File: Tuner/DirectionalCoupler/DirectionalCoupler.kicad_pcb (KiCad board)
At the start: 2 copper layers, 100 x 100 mm, 71 parts, among them J1 Conn_01x02, J10 Conn_01x01, J11 Conn_01x01, J12 Conn_01x01, J13 Conn_01x01, J14 Conn_01x01, J15 Conn_01x01, J16 Conn_01x01, J17 Barrel_Jack, J18 Conn_Coaxial, J19 Conn_01x02, J2 Conn_01x02, J20 Conn_Coaxial, J21 Conn_01x01, J22 Conn_01x01, J23 Conn_01x01, J24 Conn_01x01, J25 Conn_01x01, J26 Conn_01x01, J27 Conn_01x01, J28 Conn_01x01, J29 Conn_01x01, J3 Conn_Coaxial, J30 Conn_01x01, J31 Conn_01x01, J32 Conn_01x01, J33 Conn_01x03, J4 Conn_Coaxial, J5 Conn_01x01, J6 Conn_01x01, J7 Conn_01x01, J8 Conn_01x01, J9 Conn_01x01

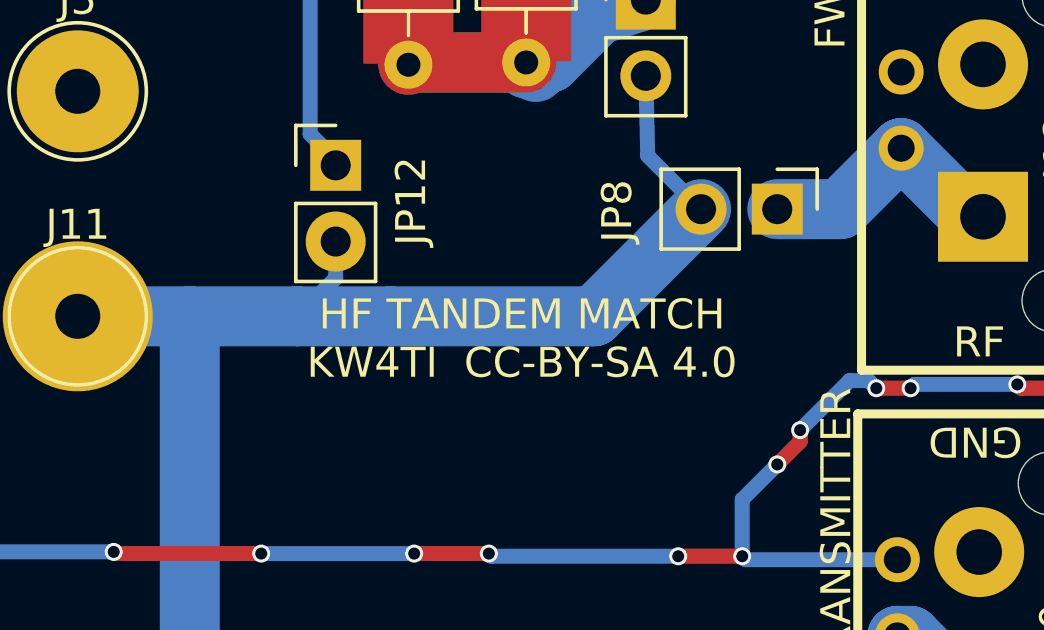
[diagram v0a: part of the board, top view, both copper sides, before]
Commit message: Change named to DirectionalCoupler, fixed order of two pins in QuadCoupler
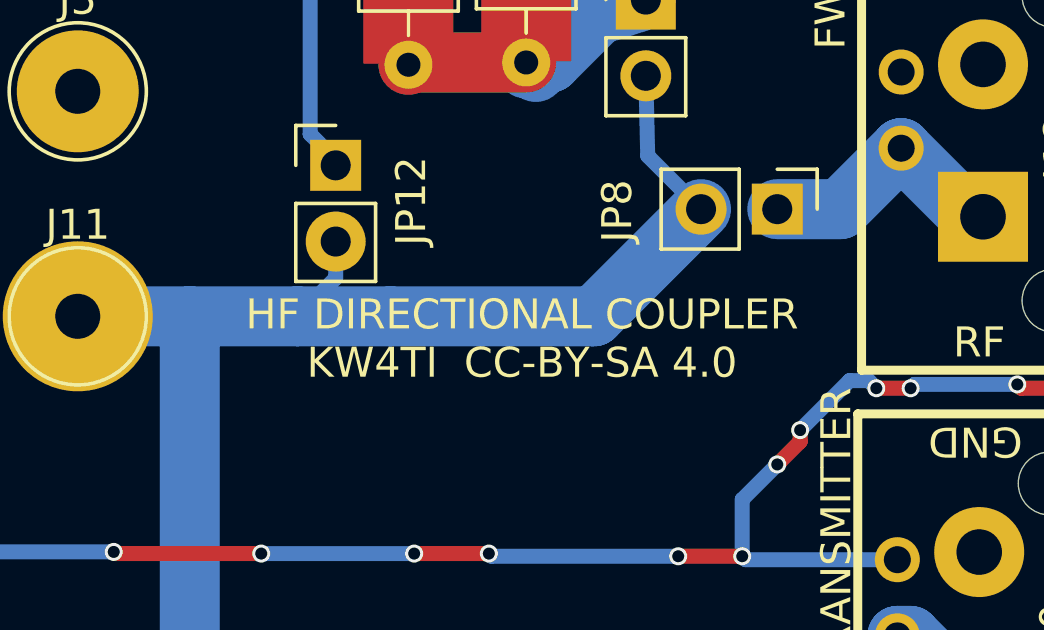
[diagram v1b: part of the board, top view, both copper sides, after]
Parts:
- F1: footprint TandemMatch:SL506Pfuseholder -> DirectionalCoupler:SL506Pfuseholder
- J18, J20, J3, J4: footprint TandemMatch:bnc_90_1-1337543-0_pad_combo -> DirectionalCoupler:bnc_90_1-1337543-0_pad_combo
- L1: footprint TandemMatch:BigRFChokeInductor -> DirectionalCoupler:BigRFChokeInductor
- R1, R2, R3, R4: footprint TandemMatch:R_Axial_DIN0309_L9.0mm_D3.2mm_P12.70mm_Horizontal -> DirectionalCoupler:R_Axial_DIN0309_L9.0mm_D3.2mm_P12.70mm_Horizontal
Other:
- board text added: "HF DIRECTIONAL COUPLER KW4TI CC-BY-SA 4.0"
- board text removed: "HF TANDEM MATCH KW4TI CC-BY-SA 4.0"
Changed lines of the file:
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@@
     (add_net "Net-(JP6-Pad1)")
   )
-  (module TandemMatch:bnc_90_1-1337543-0_pad_combo (layer F.Cu)
+  (module DirectionalCoupler:bnc_90_1-1337543-0_pad_combo (layer F.Cu)
     (at 40.386 56.769 270)
     (descr "BNC connector, Tyco 1-1337543-0")
@@
     )
   )
-  (module TandemMatch:R_Axial_DIN0309_L9.0mm_D3.2mm_P12.70mm_Horizontal (layer F.Cu)
+  (module DirectionalCoupler:R_Axial_DIN0309_L9.0mm_D3.2mm_P12.70mm_Horizontal (layer F.Cu)
     (at 111.0234 41.4147 270)
     (descr "Resistor, Axial_DIN0309 series, Axial, Horizontal, pin pitch=12.7mm, 0.5W = 1/2W, length*diameter=9*3.2mm^2, http://cdn-reichelt.de/documents/datenblatt/B400/1_4W%23YAG.pdf")
@@
     )
   )
-  (module TandemMatch:R_Axial_DIN0309_L9.0mm_D3.2mm_P12.70mm_Horizontal (layer F.Cu)
+  (module DirectionalCoupler:R_Axial_DIN0309_L9.0mm_D3.2mm_P12.70mm_Horizontal (layer F.Cu)
     (at 114.9477 41.3385 270)
     (descr "Resistor, Axial_DIN0309 series, Axial, Horizontal, pin pitch=12.7mm, 0.5W = 1/2W, length*diameter=9*3.2mm^2, http://cdn-reichelt.de/documents/datenblatt/B400/1_4W%23YAG.pdf")
@@
     )
   )
-  (module TandemMatch:R_Axial_DIN0309_L9.0mm_D3.2mm_P12.70mm_Horizontal (layer F.Cu)
+  (module DirectionalCoupler:R_Axial_DIN0309_L9.0mm_D3.2mm_P12.70mm_Horizontal (layer F.Cu)
     (at 66.4464 42.0243 270)
     (descr "Resistor, Axial_DIN0309 series, Axial, Horizontal, pin pitch=12.7mm, 0.5W = 1/2W, length*diameter=9*3.2mm^2, http://cdn-reichelt.de/documents/datenblatt/B400/1_4W%23YAG.pdf")
@@
     )
   )
-  (module TandemMatch:R_Axial_DIN0309_L9.0mm_D3.2mm_P12.70mm_Horizontal (layer F.Cu)
+  (module DirectionalCoupler:R_Axial_DIN0309_L9.0mm_D3.2mm_P12.70mm_Horizontal (layer F.Cu)
     (at 62.484 41.9862 270)
     (descr "Resistor, Axial_DIN0309 series, Axial, Horizontal, pin pitch=12.7mm, 0.5W = 1/2W, length*diameter=9*3.2mm^2, http://cdn-reichelt.de/documents/datenblatt/B400/1_4W%23YAG.pdf")
@@
     )
   )
-  (module TandemMatch:SL506Pfuseholder (layer F.Cu)
+  (module DirectionalCoupler:SL506Pfuseholder (layer F.Cu)
     (at 112.0775 109.093 270)
     (fp_text reference F1 (at 0 0 360) (layer F.SilkS)
@@
     )
   )
-  (module TandemMatch:BigRFChokeInductor (layer F.Cu)
+  (module DirectionalCoupler:BigRFChokeInductor (layer F.Cu)
     (at 130.302 107.95 90)
     (fp_text reference L1 (at -11 3 90) (layer F.SilkS)
@@
     (pad "" np_thru_hole circle (at 0 6 90) (size 4 4) (drill 4) (layers *.Cu *.Mask))
   )
-  (module TandemMatch:bnc_90_1-1337543-0_pad_combo (layer F.Cu)
+  (module DirectionalCoupler:bnc_90_1-1337543-0_pad_combo (layer F.Cu)
     (at 40.259 73.406 270)
     (descr "BNC connector, Tyco 1-1337543-0")
@@
     )
   )
-  (module TandemMatch:bnc_90_1-1337543-0_pad_combo (layer F.Cu)
+  (module DirectionalCoupler:bnc_90_1-1337543-0_pad_combo (layer F.Cu)
     (at 139.827 56.896 90)
     (descr "BNC connector, Tyco 1-1337543-0")
@@
     )
   )
-  (module TandemMatch:bnc_90_1-1337543-0_pad_combo (layer F.Cu)
+  (module DirectionalCoupler:bnc_90_1-1337543-0_pad_combo (layer F.Cu)
     (at 139.7 73.152 90)
     (descr "BNC connector, Tyco 1-1337543-0")
@@
     (effects (font (size 1 1) (thickness 0.15)))
   )
-  (gr_text "HF TANDEM MATCH\nKW4TI  CC-BY-SA 4.0" (at 114.808 63.246) (layer F.SilkS)
+  (gr_text "HF DIRECTIONAL COUPLER\nKW4TI  CC-BY-SA 4.0" (at 114.808 63.246) (layer F.SilkS)
     (effects (font (size 1 1) (thickness 0.15)))
   )

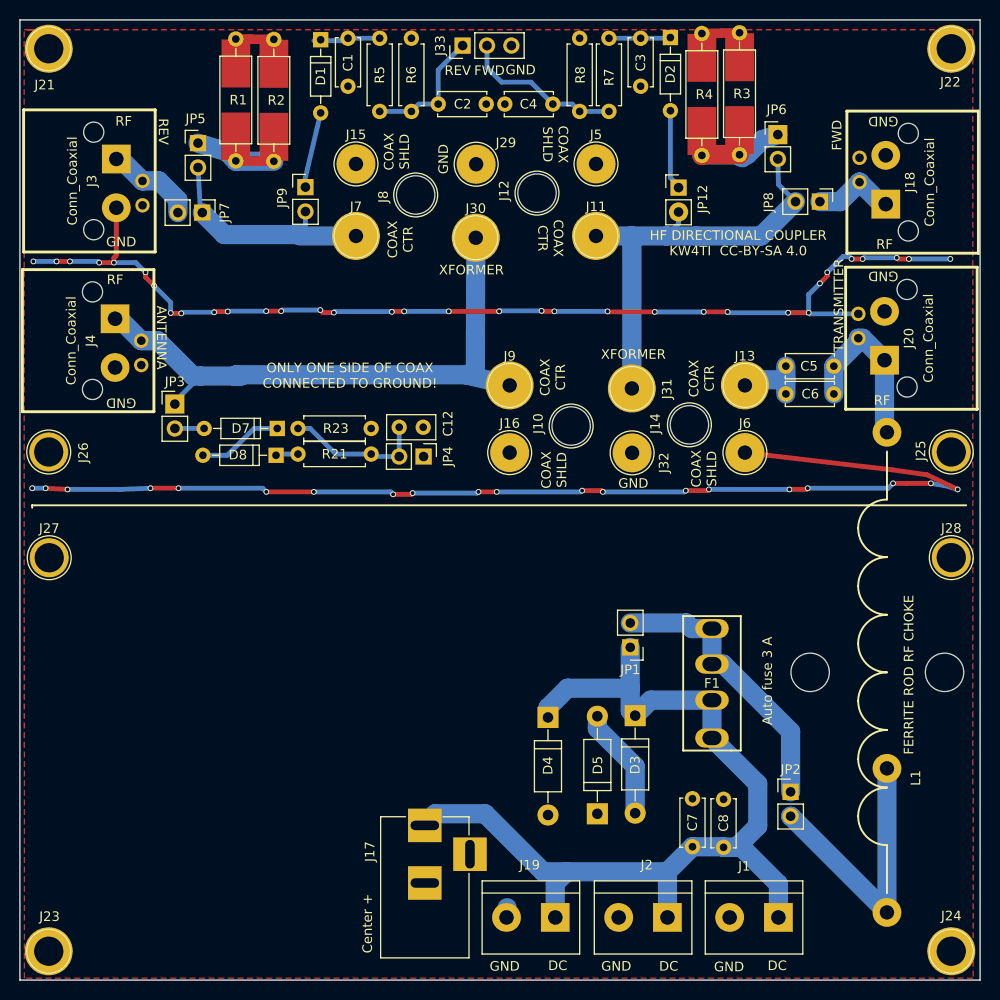
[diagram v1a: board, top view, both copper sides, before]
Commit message: Added OptoisolatedRelay
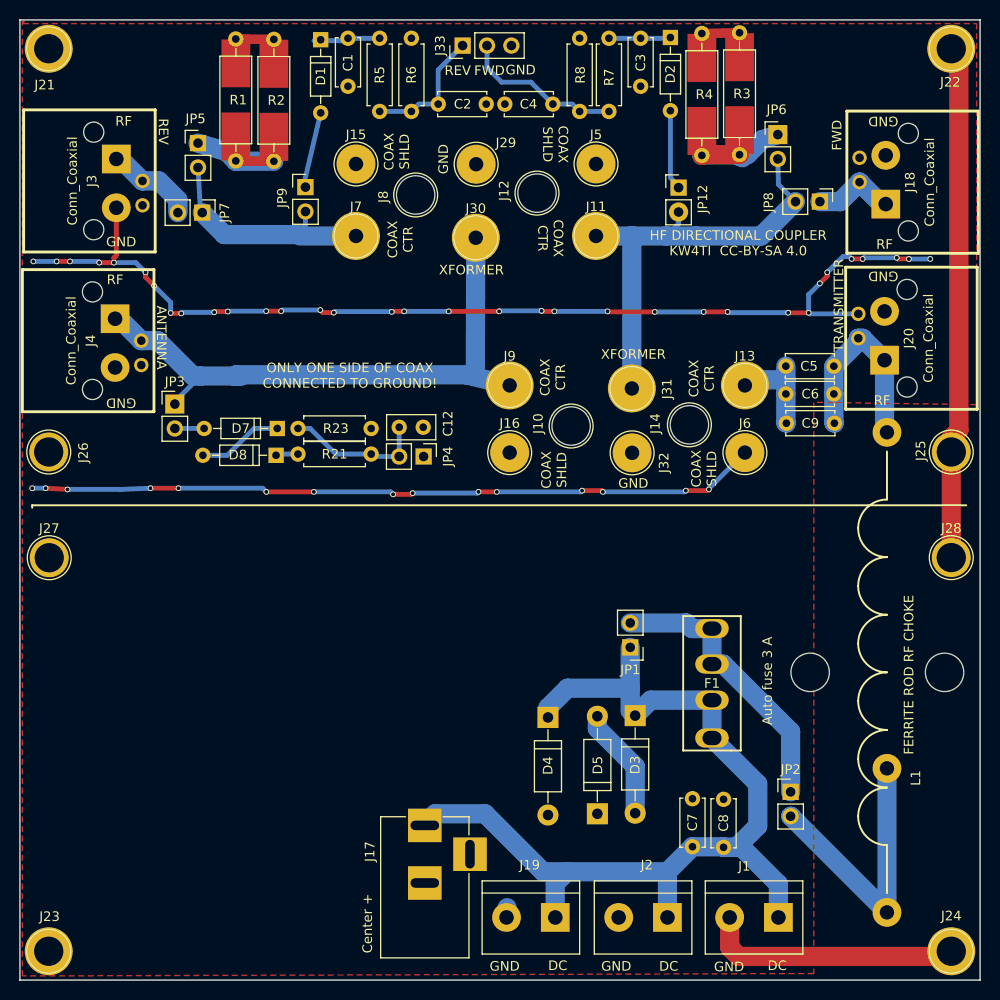
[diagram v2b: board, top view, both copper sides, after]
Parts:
- added C9: 10 nF, Capacitors_THT:C_Disc_D5.0mm_W2.5mm_P5.00mm, F.Cu at (119.8, 82.0)
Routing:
- net GND: track 253.2 -> 288.1 mm, vias 54 -> 49
- net Net-(C5-Pad2): track 18.8 -> 21.9 mm
- net Net-(C5-Pad1): track 7.40 -> 10.5 mm
